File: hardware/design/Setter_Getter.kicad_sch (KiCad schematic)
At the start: 10 parts, among them Q4801 2N7000, U4801 LM393

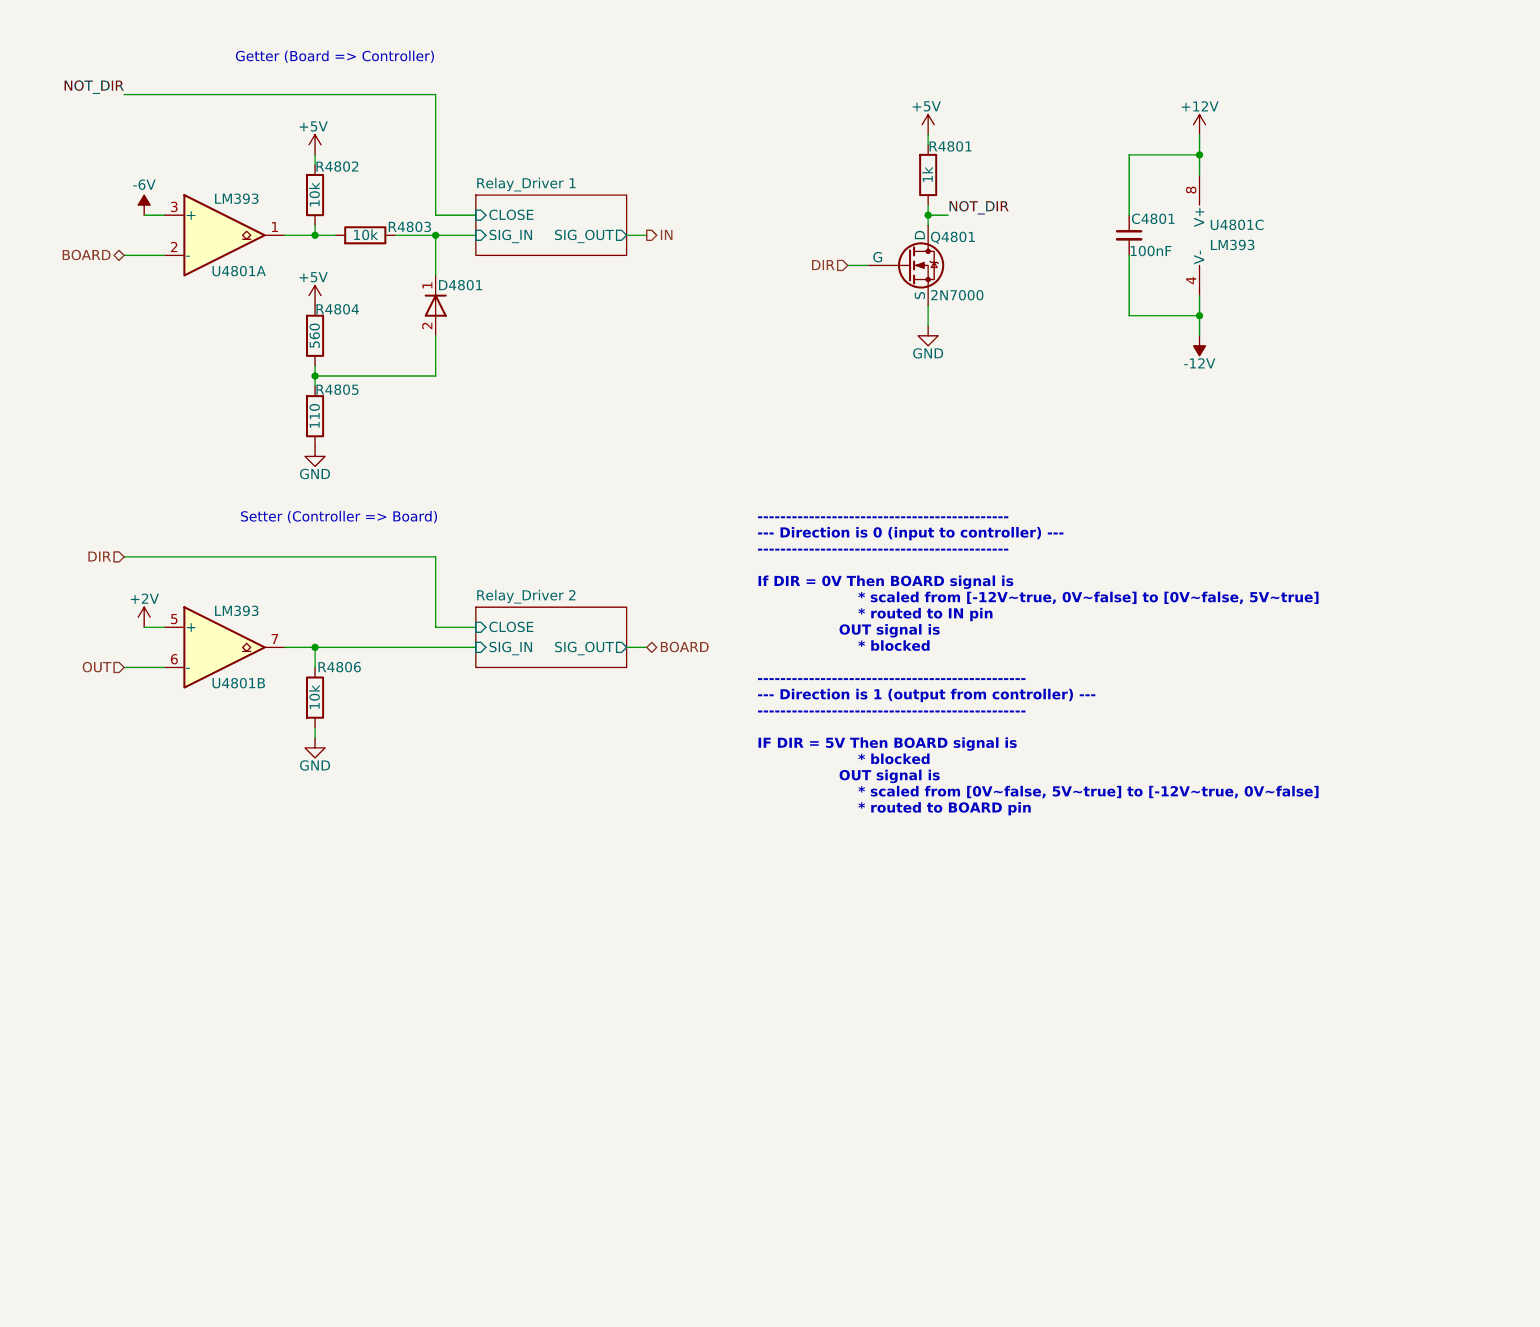
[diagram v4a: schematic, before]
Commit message: Added Setter_Getter proof of concept and Setter_Getter 74xx165 and 74xx595 integration proof of concept
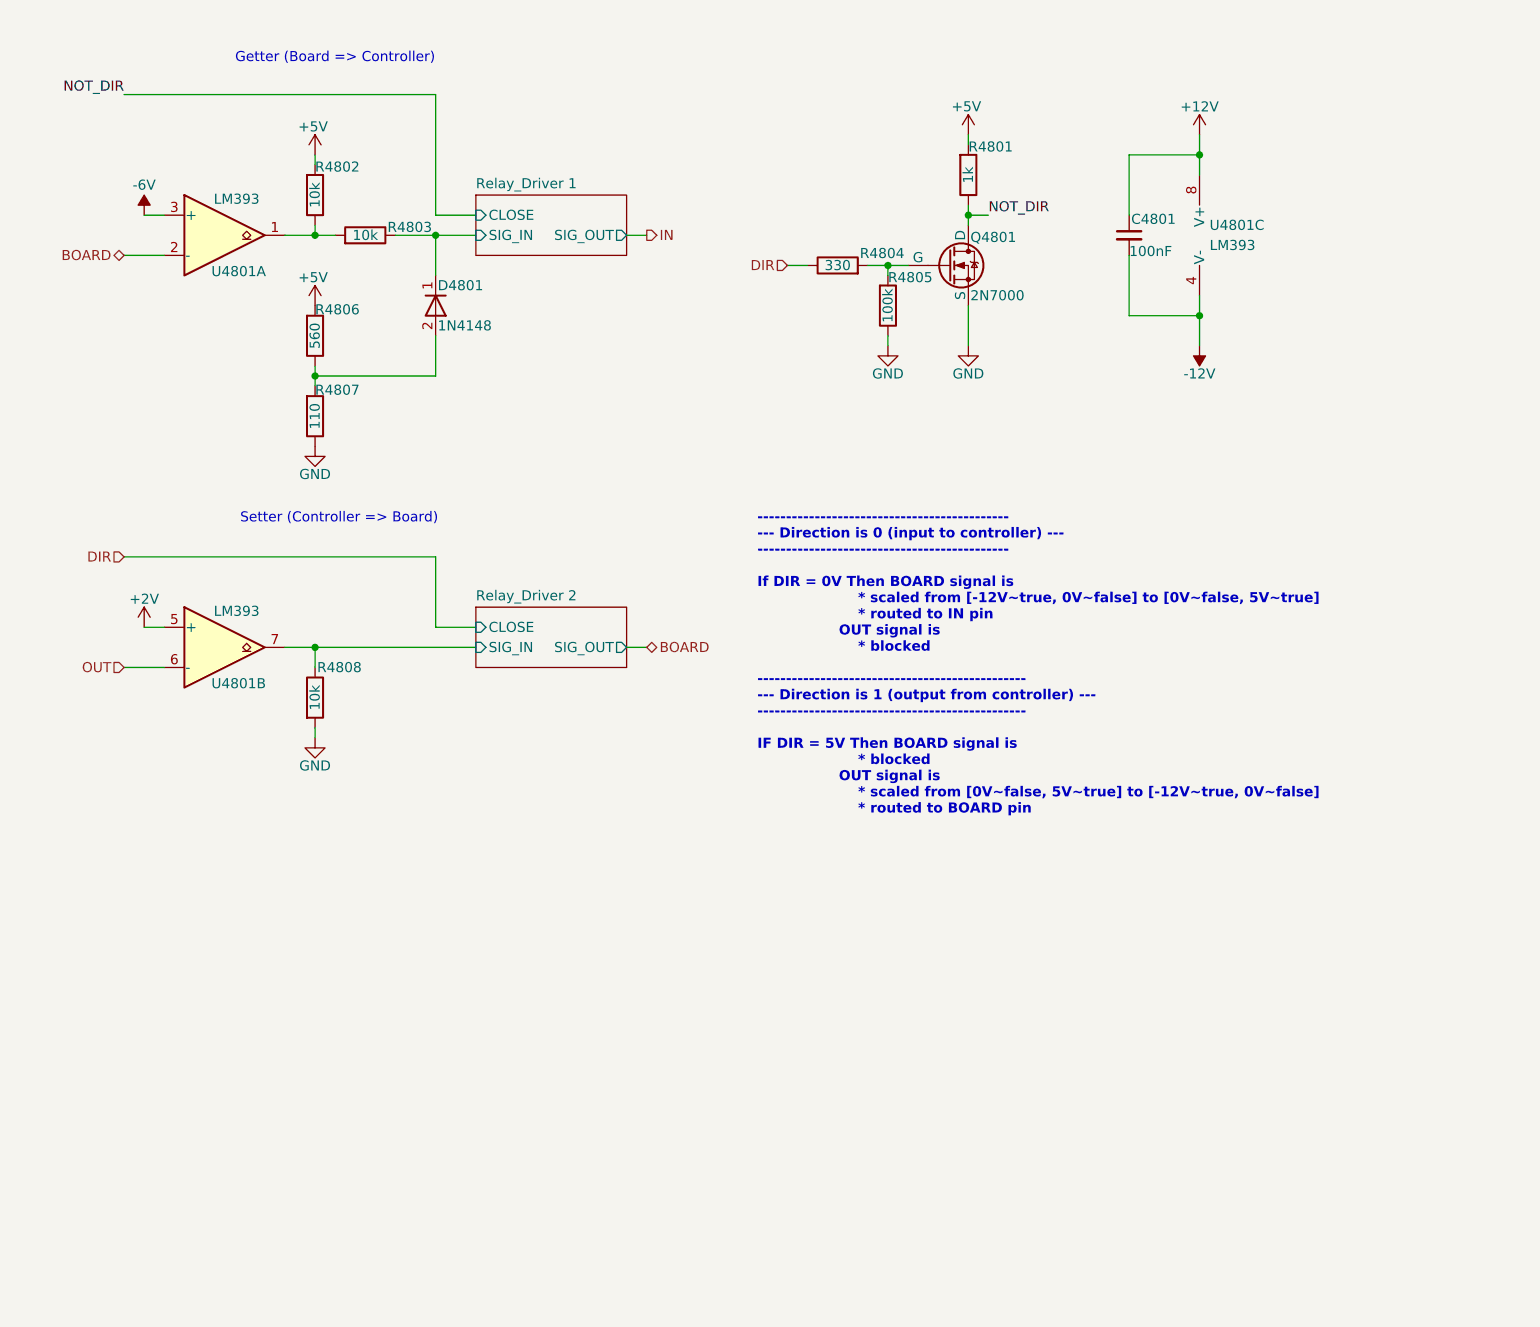
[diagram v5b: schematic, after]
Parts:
- added R4804: 330, Resistor_THT:R_Axial_DIN0207_L6.3mm_D2.5mm_P7.62mm_Horizontal, symbol Device:R
- added R4805: 100k, Resistor_THT:R_Axial_DIN0207_L6.3mm_D2.5mm_P7.62mm_Horizontal, symbol Device:R
- D4801: value D -> 1N4148
- renumbered R4804 to R4806, R4805 to R4807, R4806 to R4808
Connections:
- net DIR: now also R4804.1; no longer Q4801.2 (G)
- net GND: now also R4805.1
- new net: Q4801.2 (G), R4804.2, R4805.2
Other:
- moved on the sheet: Q4801, R4801

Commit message: File cleanup
Added final schematics
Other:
- note added: "-------------------------------------------- --- Direction is 0 (input to controller) --- -------------------------------------------- If DIR = 0V Then outgoing BOARD signal is * scaled from [-12V~true, 0V~false] to [0V~false, 5V~true] * routed to IN pin OUT signal is * blocked ----------------------------------------------- --- Direction is 1 (output from controller) --- ------------------------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"
- note removed: "-------------------------------------------- --- Direction is 0 (input to controller) --- -------------------------------------------- If DIR = 0V Then BOARD signal is * scaled from [-12V~true, 0V~false] to [0V~false, 5V~true] * routed to IN pin OUT signal is * blocked ----------------------------------------------- --- Direction is 1 (output from controller) --- ---------------------------------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"
